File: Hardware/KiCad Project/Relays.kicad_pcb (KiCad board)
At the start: 2 copper layers, 88.9 x 77.5 mm, 64 parts, among them K1 SIP-1A05, K10 SIP-1A05, K11 SIP-1A05, K12 SIP-1A05, K13 SIP-1A05, K14 SIP-1A05, K2 SIP-1A05, K3 SIP-1A05, K4 SIP-1A05, K5 SIP-1A05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

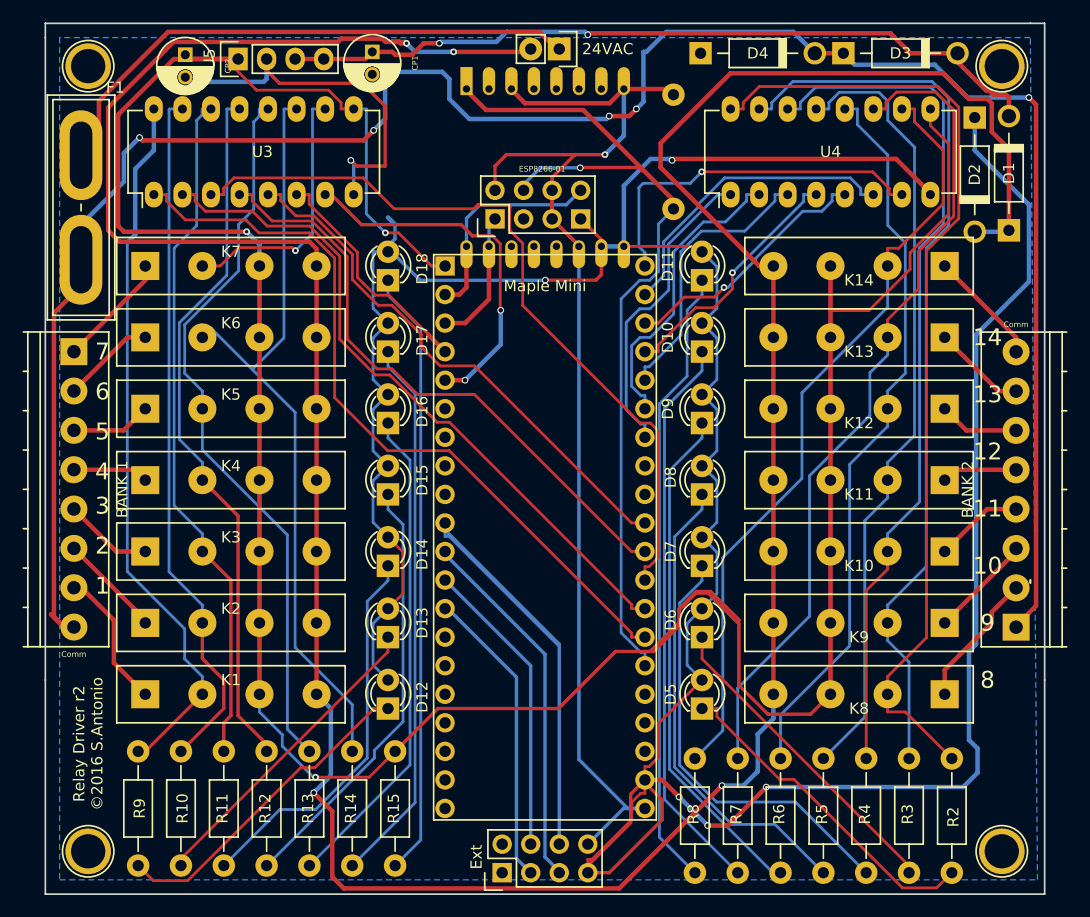
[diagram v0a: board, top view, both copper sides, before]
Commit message: tweaked silkscreen and footprints slightly
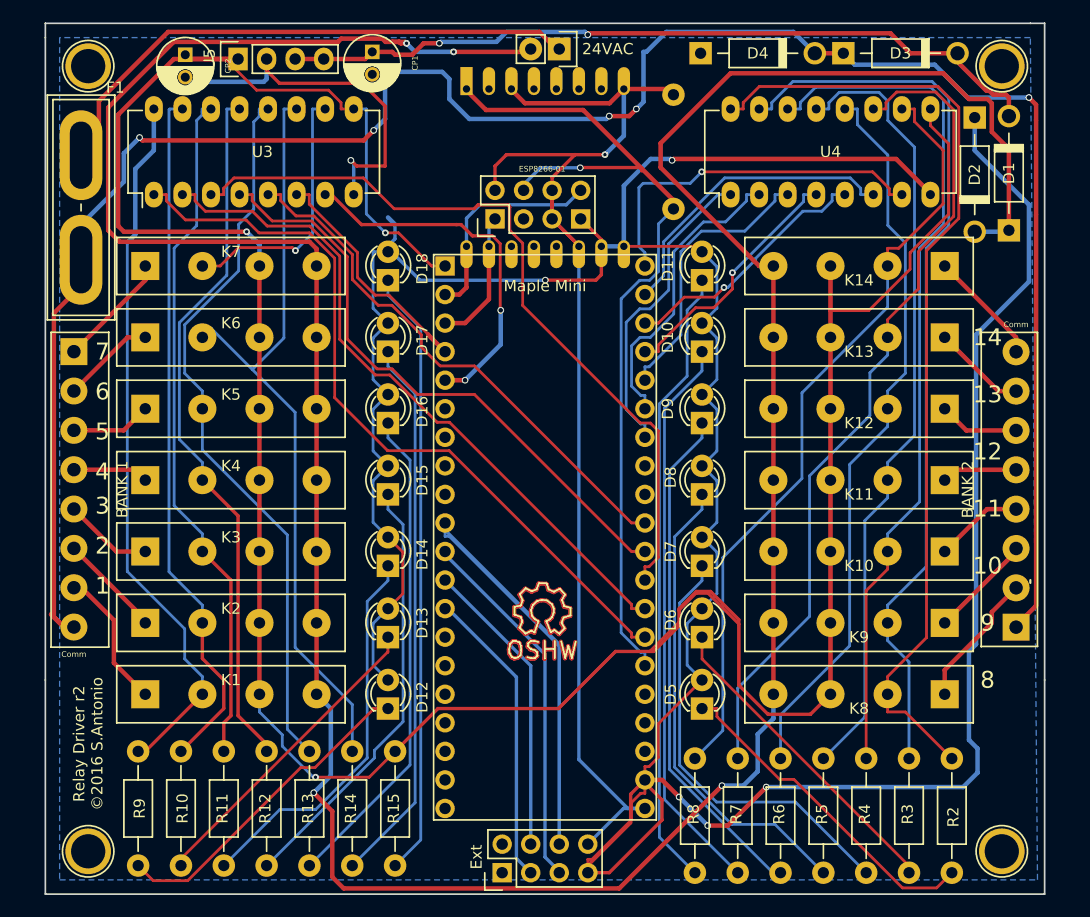
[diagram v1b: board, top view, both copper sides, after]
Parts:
- added LOGO1: Symbol_OSHW-Logo_SilkScreen, Symbols:Symbol_OSHW-Logo_SilkScreen, F.Cu at (189.0, 127.2)
- added LOGO2: Symbol_OSHW-Logo_SilkScreen, Symbols:Symbol_OSHW-Logo_SilkScreen, B.Cu at (194.3, 118.1)
- added LOGO3: Symbol_OSHW-Logo_CopperTop, Symbols:Symbol_OSHW-Logo_CopperTop, F.Cu at (189.0, 127.3)
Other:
- board text removed: "TODO - ESP02 footprint"
